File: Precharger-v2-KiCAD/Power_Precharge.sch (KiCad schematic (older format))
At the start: 18 parts

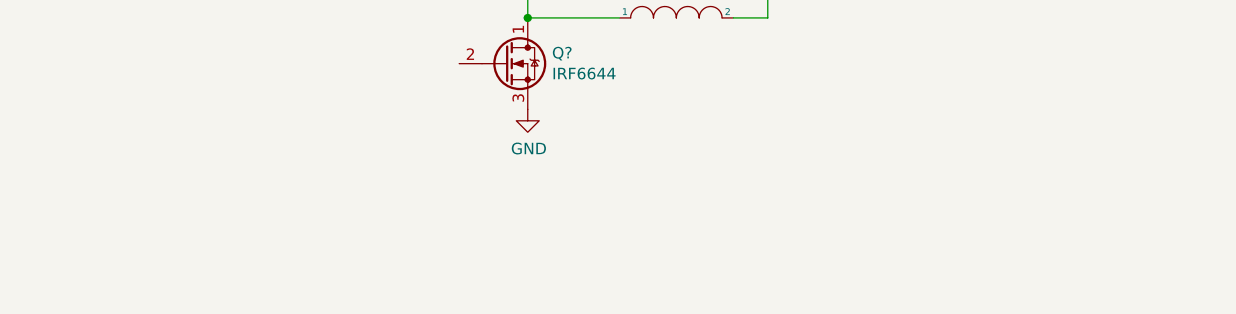
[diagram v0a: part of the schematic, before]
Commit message: Adding comment for inductor
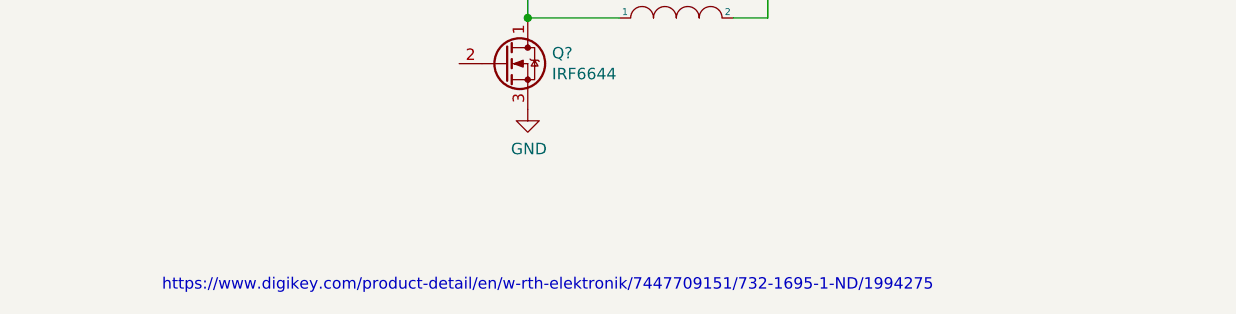
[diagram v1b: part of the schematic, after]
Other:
- note added: "https://www.digikey.com/product-detail/en/w-rth-elektronik/7447709151/732-1695-1-ND/1994275"
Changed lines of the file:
@@
 	1    0    0    -1
 $EndComp
+Text Notes 7050 6150 0    50   ~ 0
+https://www.digikey.com/product-detail/en/w-rth-elektronik/7447709151/732-1695-1-ND/1994275
 $EndSCHEMATC
